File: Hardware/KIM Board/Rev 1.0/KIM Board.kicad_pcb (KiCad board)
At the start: 2 copper layers, 280 x 220 mm, 128 parts, among them J1 KIM ENABLE, J2 DB9 FEMALE (DCE), J3 CTS EN, J4 CARD SLOT, J5 6502 BUS, J6 BREADBOARD HEADERS, J7 5V DC, Q1 2N3904, SW1 0, SW10 9, SW11 10, SW12 11, SW13 12, SW14 13, SW15 14, SW16 15, SW17 16, SW18 17, SW19 18, SW2 1, SW20 19, SW21 20, SW22 21, SW23 22, SW24 23, SW25 IO ENABLE, SW26 RESET, SW27 POWER, SW3 2, SW4 3, SW5 4, SW6 5, SW7 6, SW8 7, SW9 8, U1 65C02, U10 74HC138, U11 74HC138, U12 LM555, U13 LCD-16X2, U14 MAX232, U15 R6551AP, U16 MM74C922, U17 74HC00, U2 AS6C62256, U3 AT28C256, U4 74HC00, U5 74HC00, U6 74HC00, U7 74HC138, U8 W65C21N, U9 AT28C64, X1 1 MHz, Y1 1.8432 Mhz

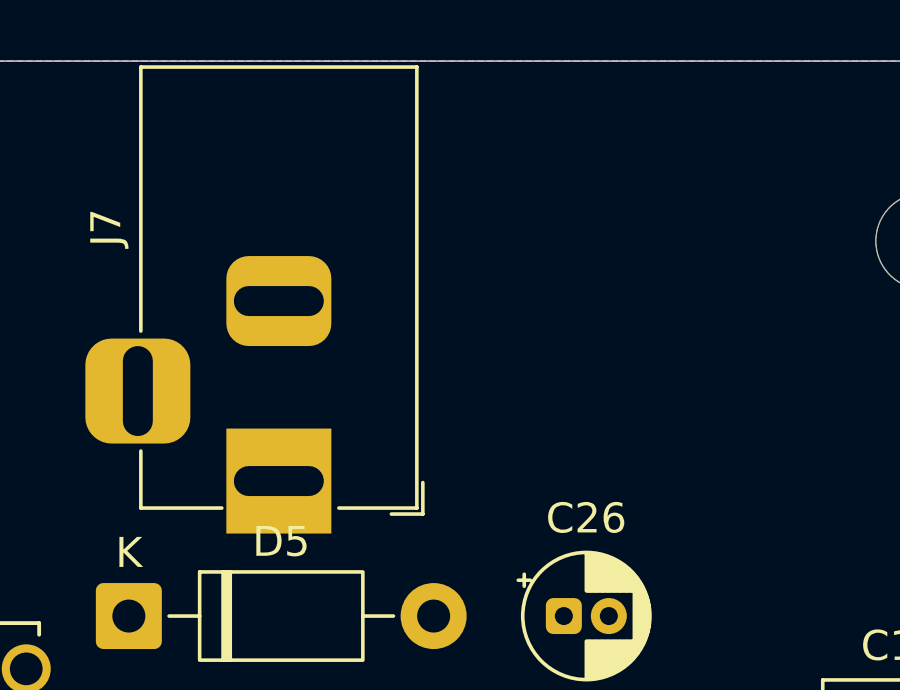
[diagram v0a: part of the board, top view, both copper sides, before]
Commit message: Add center positive symbol to barrel jack
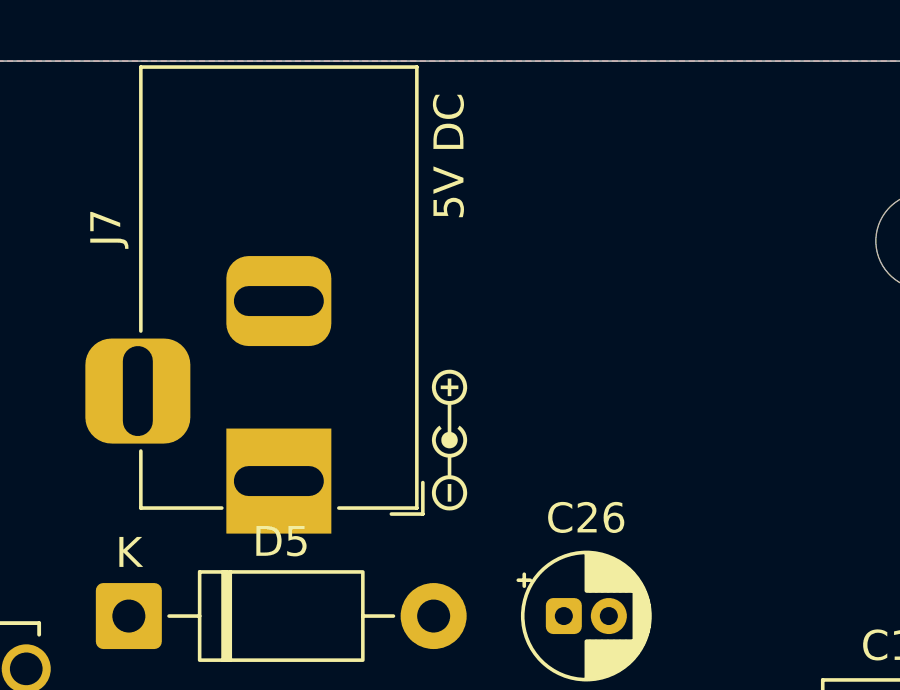
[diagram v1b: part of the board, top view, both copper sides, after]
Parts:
- added REF**: Polarity_Center_Positive_6mm_SilkScreen, Symbol:Polarity_Center_Positive_6mm_SilkScreen, F.Cu at (128.2, 87.6)
